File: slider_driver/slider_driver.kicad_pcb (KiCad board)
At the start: 2 copper layers, 15 parts, among them P1 CapRec, P2 CapSend, P3 Position, P4 IB, P5 IA, P6 +V, P7 GND, U1 L9110, U2 RSA0N11M9A0J

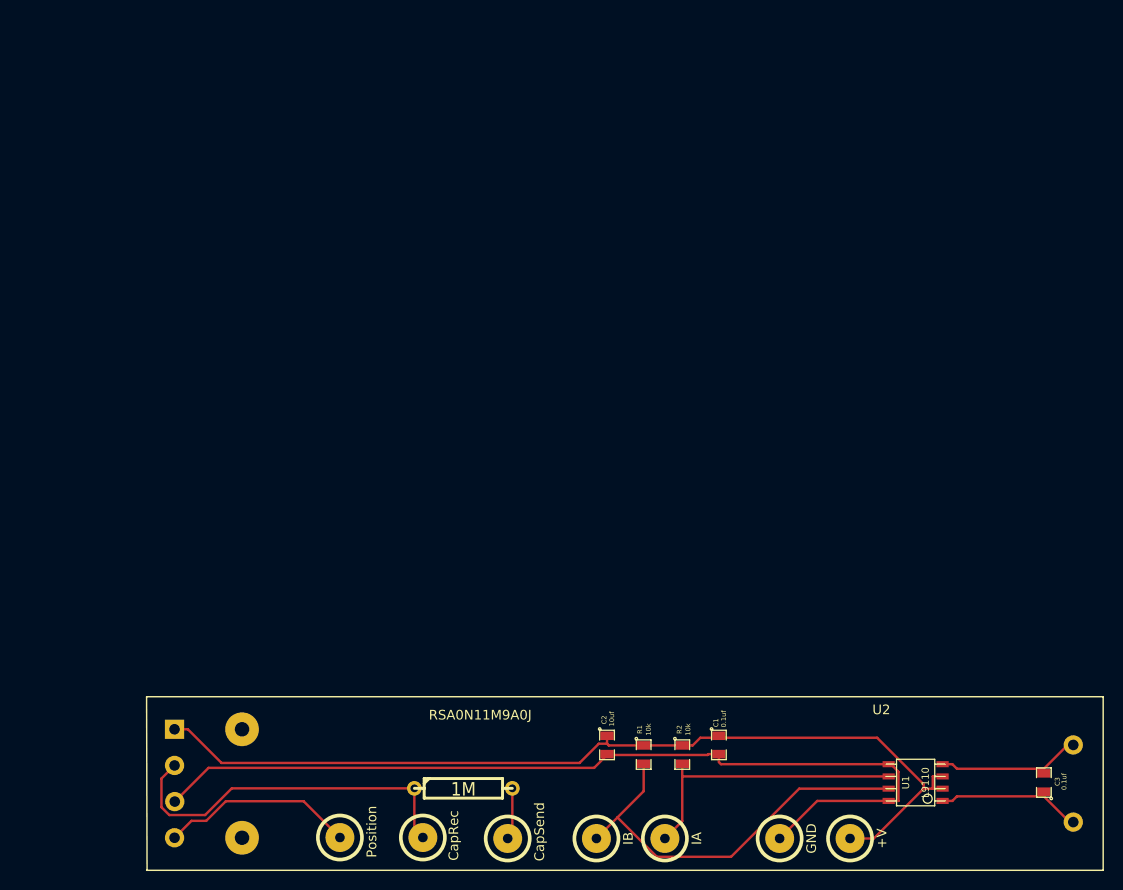
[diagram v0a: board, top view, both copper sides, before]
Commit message: added attiny to board
Bit of a feature creep here.  The board is now it's own little self
contained unit that can be accessed using i2c.
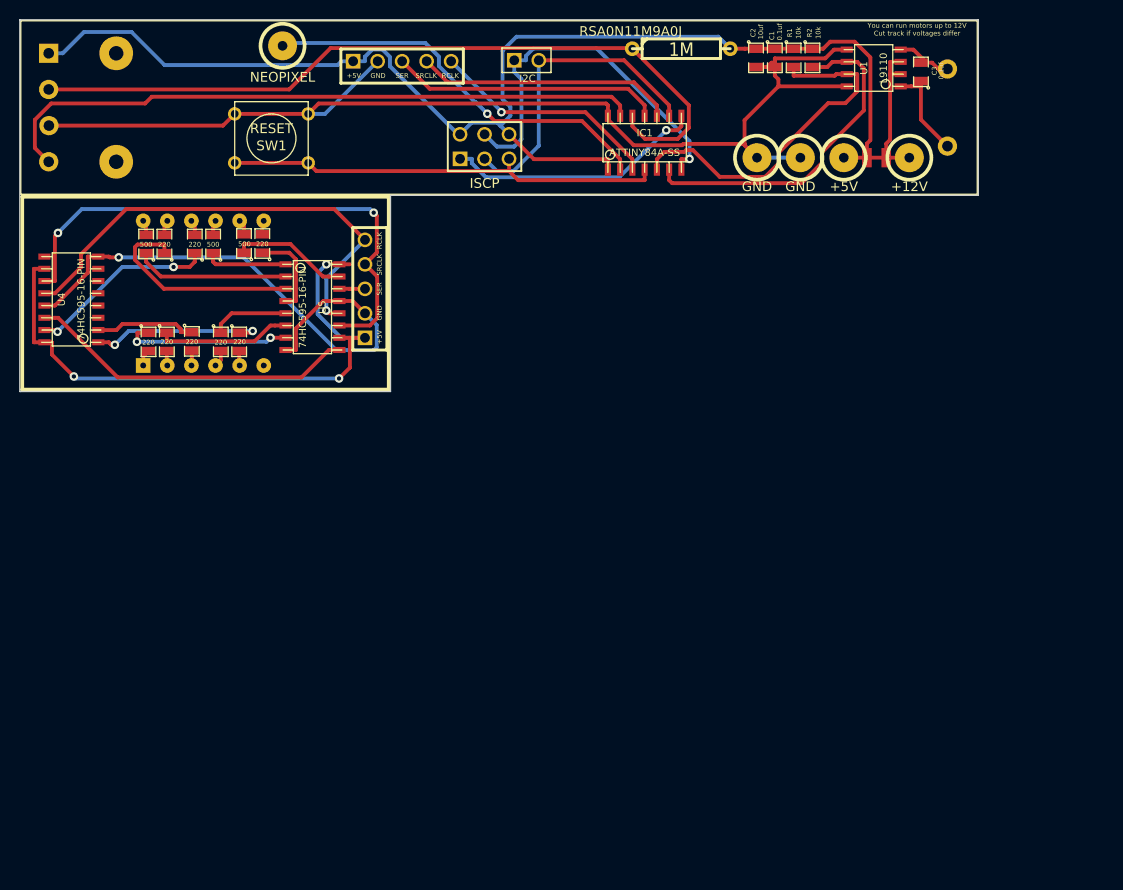
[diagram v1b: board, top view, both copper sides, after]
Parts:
- added AFF1: 3X7SEGMENTS, 3_Digit_7_Segment, F.Cu at (31.0, 40.4)
- added IC1: ATTINY84A-SS, so-14, F.Cu at (76.8, 24.8)
- added P8: +5V, 1pin_slider, F.Cu at (97.5, 26.3)
- added P9: GND, 1pin_slider, F.Cu at (93.0, 26.3)
- added R10: 220, SM0805, F.Cu at (34.8, 45.4)
- added R11: 220, SM0805, F.Cu at (29.9, 45.4)
- added R12: 500, SM0805, F.Cu at (25.1, 35.2)
- added R13: 500, SM0805, F.Cu at (32.0, 35.2)
- added R14: 500, SM0805, F.Cu at (35.2, 35.2)
- added R4: 220, SM0805, F.Cu at (27.0, 35.2)
- added R5: 220, SM0805, F.Cu at (37.1, 35.2)
- added R6: 220, SM0805, F.Cu at (32.9, 45.4)
- added R7: 220, SM0805, F.Cu at (27.2, 45.4)
- added R8: 220, SM0805, F.Cu at (25.4, 45.4)
- added R9: 220, SM0805, F.Cu at (30.1, 35.2)
- added SW1: RESET, SW_PUSH_SMALL, F.Cu at (38.1, 24.3)
- added U3: BREAK_CONNECTION, break_connection, F.Cu at (100.8, 24.3)
- added U4: 74HC595-16-PIN, so-16, F.Cu at (17.4, 41.0)
- added U5: 74HC595-16-PIN, so-16, F.Cu at (42.4, 41.8)
- P1: value CapRec -> 5_PIN_SOCKET; footprint 1pin_slider -> 5pin_display
- P2: value CapSend -> NEOPIXEL
- P3: value Position -> 5_PIN_SOCKET; footprint 1pin_slider -> 5pin_display
- P4: value IB -> I2C; footprint 1pin_slider -> PIN_ARRAY_2X1
- P5: value IA -> ISCP; footprint 1pin_slider -> pin_array_3x2
- P6: value +V -> +12V
- moved P2 85.5 mm to (39.2, 14.7)
- moved P4 81.0 mm to (64.5, 16.2)
- moved P1 80.5 mm to (51.6, 16.3)
- moved R3 80.0 mm to (80.6, 15.0)
- moved C3 74.8 mm to (105.5, 17.4)
- moved U1 74.2 mm to (100.5, 17.0)
- moved P5 74.1 mm to (60.2, 25.1)
- moved R1 73.9 mm to (92.2, 15.9)
- moved R2 73.5 mm to (94.2, 15.9)
- moved C2 72.9 mm to (88.3, 15.9)
- moved C1 71.5 mm to (90.3, 15.9)
- moved U2 71.3 mm to (78.7, 21.1)
- moved P6 70.9 mm to (104.2, 26.3)
- moved P7 70.6 mm to (88.5, 26.3)
- moved P3 57.0 mm to (47.8, 39.9), turned to 90 degrees
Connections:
- C1 pad 1: +5V -> +12V
- C2 pad 1: +5V -> +12V
- P1 pad 1: N-000009 -> +12V
- P2 pad 1: N-000008 -> N-0000048
- P3 pad 1: N-000007 -> N-0000015
- P4 pad 1: N-000004 -> N-0000053
- P5 pad 1: N-000003 -> N-0000045
- P6 pad 1: +5V -> +12V
- R1 pad 1: +5V -> +12V
- R1 pad 2: N-000004 -> N-0000046
- R2 pad 1: +5V -> +12V
- R2 pad 2: N-000003 -> N-0000051
- R3 pad 1: N-000009 -> N-0000049
- R3 pad 2: N-000008 -> +12V
- U1 pad 2: +5V -> +12V
- U1 pad 3: +5V -> +12V
- U1 pad 6: N-000003 -> N-0000051
- U1 pad 7: N-000004 -> N-0000046
- U2 pad 1: +5V -> +12V
- U2 pad 2: N-000007 -> N-0000050
- U2 pad T: N-000009 -> N-0000049
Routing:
- net +12V: track 0.00 -> 147.1 mm
- net +5V: track 97.9 -> 0.00 mm
- net N-0000049: track 0.00 -> 80.9 mm
- net N-0000050: track 0.00 -> 68.1 mm
- net N-0000015: track 0.00 -> 63.9 mm, vias 0 -> 3
- net N-0000014: track 0.00 -> 57.9 mm, vias 0 -> 1
- net N-0000012: track 0.00 -> 56.5 mm, vias 0 -> 2
- net N-0000019: track 0.00 -> 49.5 mm, vias 0 -> 1
- net N-0000018: track 0.00 -> 45.6 mm
- net N-000004: track 42.5 -> 0.00 mm
- net N-0000048: track 0.00 -> 41.8 mm, vias 0 -> 1
- net N-0000053: track 0.00 -> 39.9 mm, vias 0 -> 1
- net N-000009: track 38.1 -> 0.00 mm
- net N-0000046: track 0.00 -> 37.1 mm
- net N-0000051: track 0.00 -> 35.4 mm
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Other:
- board outline added: 99.4 x 38.5 mm
- board text added: "Controller for RSA0N11M9A0J motorised slider Designed by John Spencer, 2014 https://github.com/mage0r/RSA0N11M9A0J_motorised_slider Version 1.2"
- board text added: "You can run motors up to 12V Cut track if voltages differ"
- board text removed: "Controller for RSA0N11M9A0J motorised slider Designed by John Spencer, 2014 https://github.com/mage0r/RSA0N11M9A0J_motorised_slider Version 1.1"
